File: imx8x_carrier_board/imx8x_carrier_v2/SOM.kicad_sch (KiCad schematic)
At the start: 42 parts, among them J1 BTH-070-02-L-D-A, J4 BTH-070-02-L-D-A

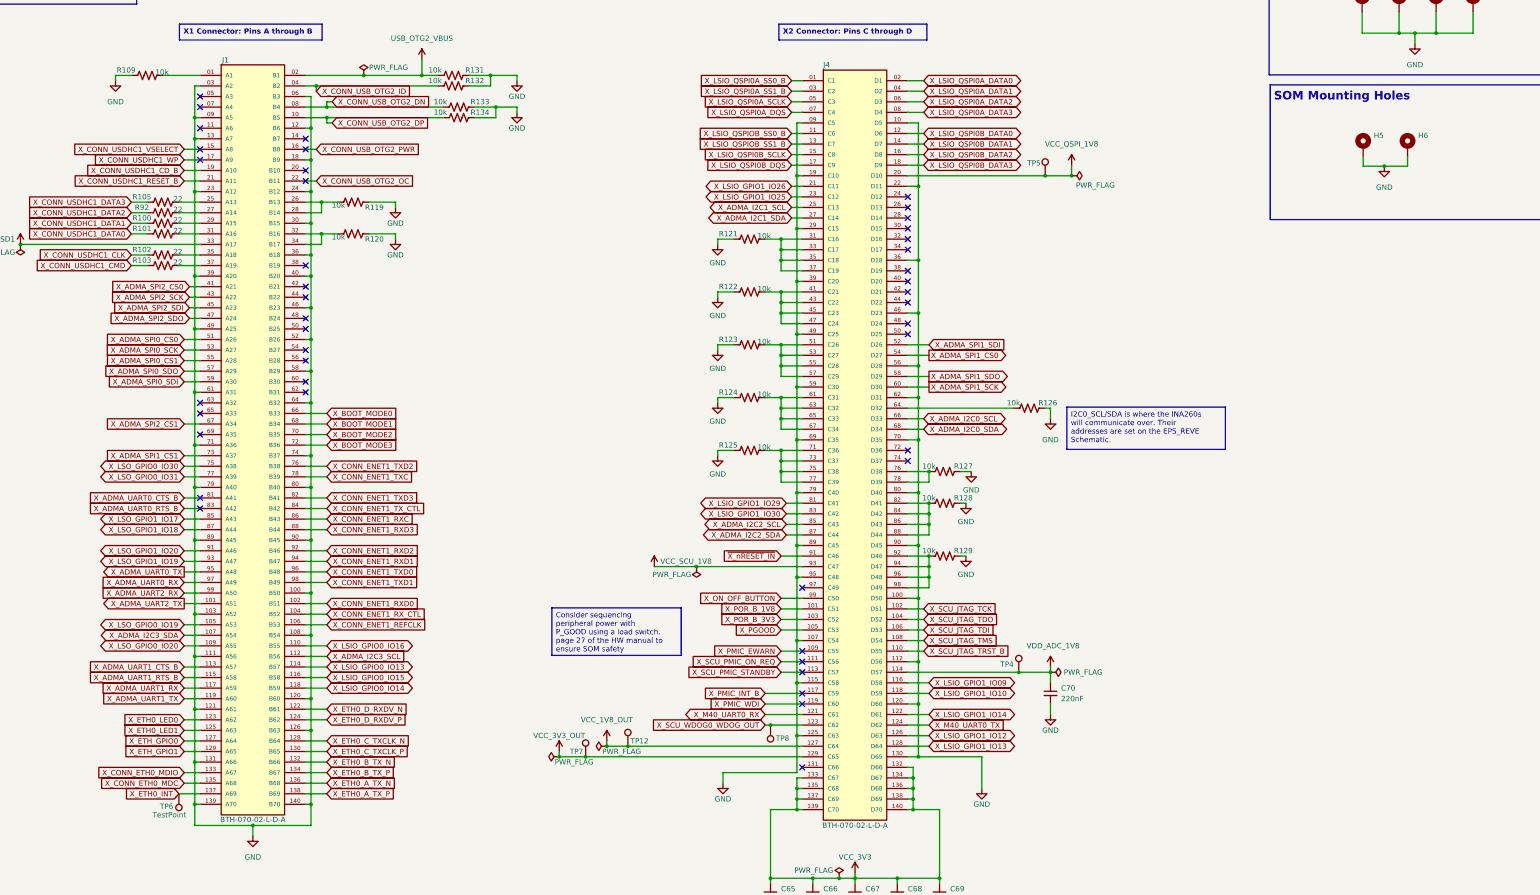
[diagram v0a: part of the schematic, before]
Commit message: Layout Changes
Consolidated the BOM a little bit, have to rerout
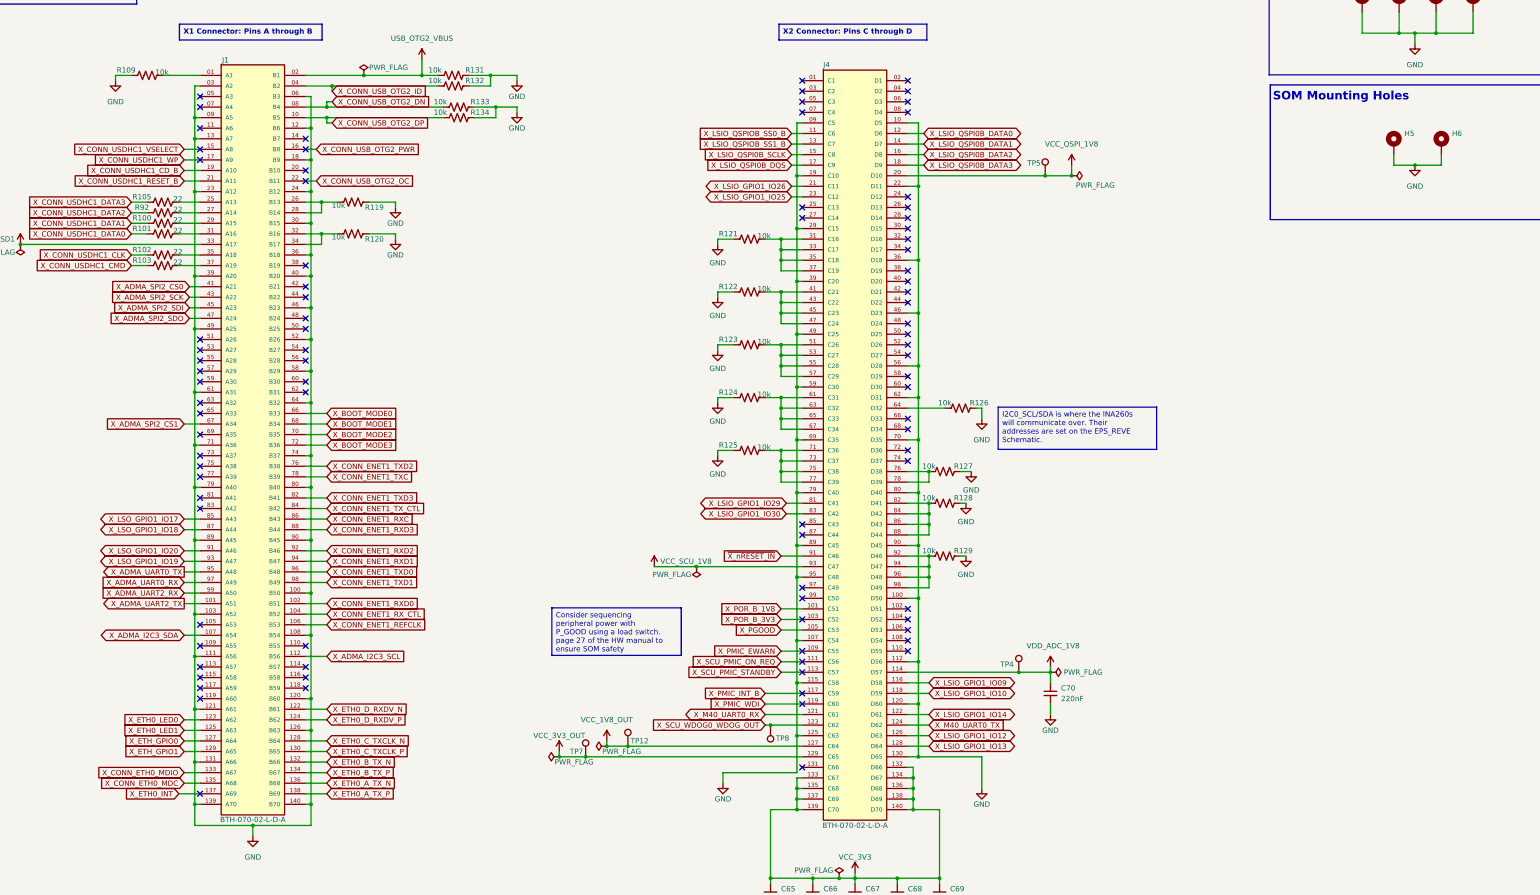
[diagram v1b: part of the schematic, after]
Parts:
- removed TP6: TestPoint, TestPoint:TestPoint_THTPad_1.0x1.0mm_Drill0.5mm, symbol Connector:TestPoint
- H1, H2, H3, H4: value MountingHole_Pad_M2.5_2.7mm -> M3
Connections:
- net X_ADMA_I2C0_SCL: no longer names the net of J4.66 (D33)
- net X_ADMA_I2C0_SDA: no longer names the net of J4.68 (D34)
- net X_ADMA_I2C1_SCL: no longer names the net of J4.25 (C13)
- net X_ADMA_I2C1_SDA: no longer names the net of J4.27 (C14)
- net X_ADMA_I2C2_SCL: no longer names the net of J4.85 (C43)
- net X_ADMA_I2C2_SDA: no longer names the net of J4.87 (C44)
- net X_ADMA_SPI0_CS0: no longer names the net of J1.51 (A26)
- net X_ADMA_SPI0_CS1: no longer names the net of J1.55 (A28)
- net X_ADMA_SPI0_SCK: no longer names the net of J1.53 (A27)
- net X_ADMA_SPI0_SDI: no longer names the net of J1.59 (A30)
- net X_ADMA_SPI0_SDO: no longer names the net of J1.57 (A29)
- net X_ADMA_SPI1_CS0: no longer names the net of J4.54 (D27)
- net X_ADMA_SPI1_CS1: no longer names the net of J1.73 (A37)
- net X_ADMA_SPI1_SCK: no longer names the net of J4.60 (D30)
- net X_ADMA_SPI1_SDI: no longer names the net of J4.52 (D26)
- net X_ADMA_SPI1_SDO: no longer names the net of J4.58 (D29)
- net X_ADMA_UART0_CTS_B: no longer names the net of J1.81 (A41)
- net X_ADMA_UART0_RTS_B: no longer names the net of J1.83 (A42)
- net X_ADMA_UART1_CTS_B: no longer names the net of J1.113 (A57)
- net X_ADMA_UART1_RTS_B: no longer names the net of J1.115 (A58)
- net X_ADMA_UART1_RX: no longer names the net of J1.117 (A59)
- net X_ADMA_UART1_TX: no longer names the net of J1.119 (A60)
- net X_LSIO_GPIO0_IO13: no longer names the net of J1.114 (B57)
- net X_LSIO_GPIO0_IO14: no longer names the net of J1.118 (B59)
- net X_LSIO_GPIO0_IO15: no longer names the net of J1.116 (B58)
- net X_LSIO_GPIO0_IO16: no longer names the net of J1.110 (B55)
- net X_LSIO_QSPI0A_DATA0: no longer names the net of J4.02 (D1)
- net X_LSIO_QSPI0A_DATA1: no longer names the net of J4.04 (D2)
- net X_LSIO_QSPI0A_DATA2: no longer names the net of J4.06 (D3)
- net X_LSIO_QSPI0A_DATA3: no longer names the net of J4.08 (D4)
- net X_LSIO_QSPI0A_DQS: no longer names the net of J4.07 (C4)
- net X_LSIO_QSPI0A_SCLK: no longer names the net of J4.05 (C3)
- net X_LSIO_QSPI0A_SS0_B: no longer names the net of J4.01 (C1)
- net X_LSIO_QSPI0A_SS1_B: no longer names the net of J4.03 (C2)
- net X_LSO_GPIO0_IO19: no longer names the net of J1.105 (A53)
- net X_LSO_GPIO0_IO20: no longer names the net of J1.109 (A55)
- net X_LSO_GPIO0_IO30: no longer names the net of J1.75 (A38)
- net X_LSO_GPIO0_IO31: no longer names the net of J1.77 (A39)
- net X_ON_OFF_BUTTON: no longer names the net of J4.99 (C50)
- net X_SCU_JTAG_TCK: no longer names the net of J4.102 (D51)
- net X_SCU_JTAG_TDI: no longer names the net of J4.106 (D53)
- net X_SCU_JTAG_TDO: no longer names the net of J4.104 (D52)
- net X_SCU_JTAG_TMS: no longer names the net of J4.108 (D54)
- net X_SCU_JTAG_TRST_B: no longer names the net of J4.110 (D55)
- no-connect marks 44 -> 88
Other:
- moved on the sheet: H5, H6, R126

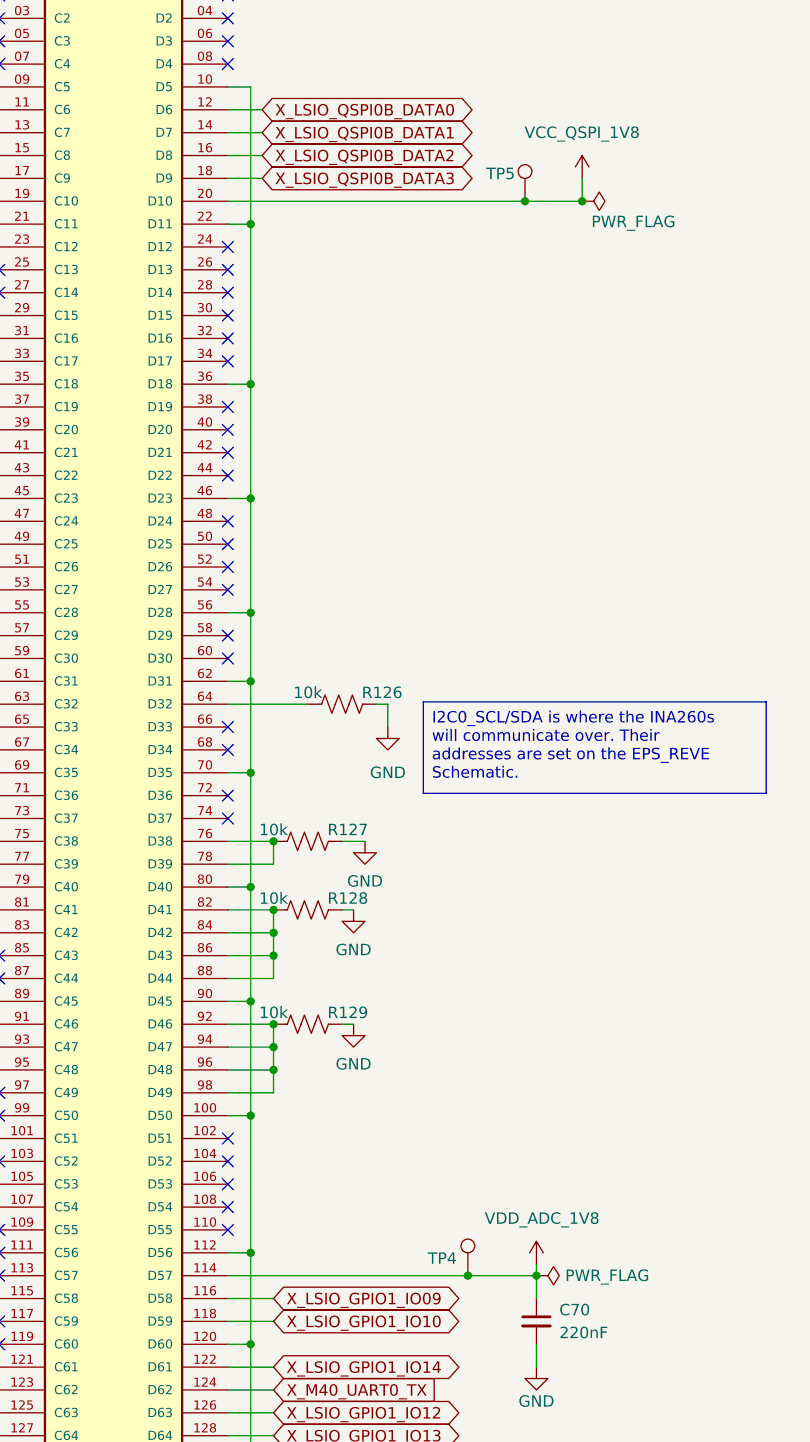
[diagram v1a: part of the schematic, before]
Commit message: Finished Routing.
Completed routing and zone fills. Fixed some parts of the schematic as well.
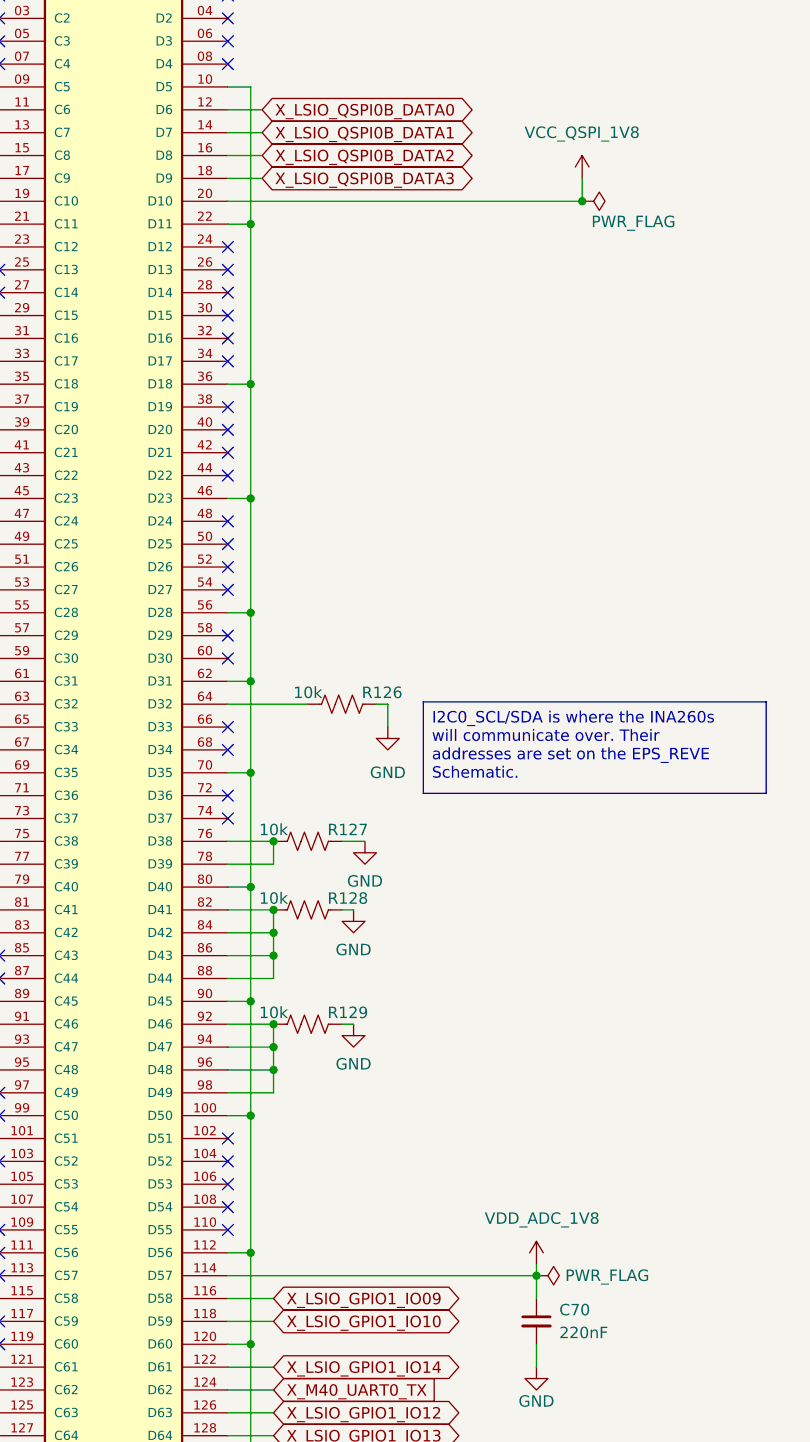
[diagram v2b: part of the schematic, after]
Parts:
- removed TP4, TP5: TestPoint, TestPoint:TestPoint_THTPad_1.0x1.0mm_Drill0.5mm, symbol Connector:TestPoint
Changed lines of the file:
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@@
 	)
 	(junction
-		(at 273.05 190.5)
-		(diameter 0)
-		(color 0 0 0 0)
-	)
-	(junction
 		(at 74.93 212.09)
 		(diameter 0)
@@
 	)
 	(junction
-		(at 279.4 71.12)
-		(diameter 0)
-		(color 0 0 0 0)
-	)
-	(junction
 		(at 248.92 187.96)
 		(diameter 0)
@@
 	(wire
 		(pts
-			(xy 246.38 190.5) (xy 273.05 190.5)
-		)
-		(stroke
-			(width 0)
-			(type default)
-		)
-	)
-	(wire
-		(pts
 			(xy 59.69 77.47) (xy 63.5 77.47)
 		)
@@
 	(wire
 		(pts
-			(xy 273.05 190.5) (xy 280.67 190.5)
+			(xy 246.38 190.5) (xy 280.67 190.5)
 		)
 		(stroke
@@
 	(wire
 		(pts
-			(xy 279.4 71.12) (xy 246.38 71.12)
+			(xy 246.38 71.12) (xy 285.75 71.12)
 		)
 		(stroke
@@
 	(wire
 		(pts
-			(xy 279.4 71.12) (xy 285.75 71.12)
-		)
-		(stroke
-			(width 0)
-			(type default)
-		)
-	)
-	(wire
-		(pts
 			(xy 76.2 49.53) (xy 74.93 49.53)
 		)
@@
 	)
 	(symbol
-		(lib_id "Connector:TestPoint")
-		(at 279.4 71.12 0)
-		(unit 1)
-		(exclude_from_sim no)
-		(in_bom yes)
-		(on_board yes)
-		(dnp no)
-		(property "Reference" "TP5"
-			(at 275.082 68.072 0)
-			(effects
-				(font
-					(size 1.27 1.27)
-				)
-				(justify left)
-			)
-		)
-		(property "Value" "TestPoint"
-			(at 269.875 69.85 0)
-			(effects
-				(font
-					(size 1.27 1.27)
-				)
-				(justify left)
-				(hide yes)
-			)
-		)
-		(property "Footprint" "TestPoint:TestPoint_THTPad_1.0x1.0mm_Drill0.5mm"
-			(at 284.48 71.12 0)
-			(effects
-				(font
-					(size 1.27 1.27)
-				)
-				(hide yes)
-			)
-		)
-		(property "Datasheet" "~"
-			(at 284.48 71.12 0)
-			(effects
-				(font
-					(size 1.27 1.27)
-				)
-				(hide yes)
-			)
-		)
-		(property "Description" "test point"
-			(at 279.4 71.12 0)
-			(effects
-				(font
-					(size 1.27 1.27)
-				)
-				(hide yes)
-			)
-		)
-		(property "LCSC" ""
-			(at 279.4 71.12 0)
-			(effects
-				(font
-					(size 1.27 1.27)
-				)
-			)
-		)
-		(property "Voltage" ""
-			(at 279.4 71.12 0)
-			(effects
-				(font
-					(size 1.27 1.27)
-				)
-			)
-		)
-		(pin "1"
-		)
-		(instances
-			(project "imx8x_carrier_v1"
-				(path "/4409cb5c-c5cc-45e5-ba22-666413441047/bd9bf2b1-2646-4f47-8b43-7734a13ea490"
-					(reference "TP5")
-					(unit 1)
-				)
-			)
-		)
-	)
-	(symbol
 		(lib_id "power:PWR_FLAG")
 		(at 115.57 46.99 0)
@@
 					(unit 1)
 				)
-			)
-		)
-	)
-	(symbol
-		(lib_id "Connector:TestPoint")
-		(at 273.05 190.5 0)
-		(unit 1)
-		(exclude_from_sim no)
-		(in_bom yes)
-		(on_board yes)
-		(dnp no)
-		(property "Reference" "TP4"
-			(at 268.605 188.595 0)
-			(effects
-				(font
-					(size 1.27 1.27)
-				)
-				(justify left)
-			)
-		)
-		(property "Value" "TestPoint"
-			(at 261.62 189.23 0)
-			(effects
-				(font
-					(size 1.27 1.27)
-				)
-				(justify left)
-				(hide yes)
-			)
-		)
-		(property "Footprint" "TestPoint:TestPoint_THTPad_1.0x1.0mm_Drill0.5mm"
-			(at 278.13 190.5 0)
-			(effects
-				(font
-					(size 1.27 1.27)
-				)
-				(hide yes)
-			)
-		)
-		(property "Datasheet" "~"
-			(at 278.13 190.5 0)
-			(effects
-				(font
-					(size 1.27 1.27)
-				)
-				(hide yes)
-			)
-		)
-		(property "Description" "test point"
-			(at 273.05 190.5 0)
-			(effects
-				(font
-					(size 1.27 1.27)
-				)
-				(hide yes)
-			)
-		)
-		(property "LCSC" ""
-			(at 273.05 190.5 0)
-			(effects
-				(font
-					(size 1.27 1.27)
-				)
-			)
-		)
-		(property "Voltage" ""
-			(at 273.05 190.5 0)
-			(effects
-				(font
-					(size 1.27 1.27)
-				)
-			)
-		)
-		(pin "1"
-		)
-		(instances
-			(project "imx8x_carrier_v1"
-				(path "/4409cb5c-c5cc-45e5-ba22-666413441047/bd9bf2b1-2646-4f47-8b43-7734a13ea490"
-					(reference "TP4")
-					(unit 1)
-				)

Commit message: Fixed Minor things
Fixed SOM Position
Fixed Mounting Hole Sizes
Updated Gerbers
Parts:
- H1, H2, H3, H4: footprint MountingHole:MountingHole_2.7mm_M2.5_DIN965_Pad -> MountingHole:MountingHole_3.2mm_M3_ISO7380_Pad

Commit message: imx changes
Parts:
- added TP1, TP2: TestPoint, TestPoint:TestPoint_THTPad_1.0x1.0mm_Drill0.5mm, symbol Connector:TestPoint
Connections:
- net X_ETH0_INT: now also TP1.1
- net X_POR_B_3V3: now also TP2.1
- net USB_OTG2_VBUS: no longer names the net of J1.02 (B1), R131.2
- net X_CONN_USB_OTG2_DN: no longer names the net of J1.08 (B4), R133.2
- net X_CONN_USB_OTG2_DP: no longer names the net of J1.10 (B5), R134.2
- net X_CONN_USB_OTG2_ID: no longer names the net of J1.04 (B2), R132.2
- net X_CONN_USB_OTG2_OC: no longer names the net of J1.22 (B11)
- net X_CONN_USB_OTG2_PWR: no longer names the net of J1.16 (B8)
- net X_CONN_USDHC1_WP: no longer names the net of J1.17 (A9)
- no-connect marks 88 -> 86
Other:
- note added: "Switch the watchdog and the m40 uart"
